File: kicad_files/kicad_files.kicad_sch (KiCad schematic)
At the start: 12 parts, among them J1 Battery Connection, J2 Servo Connection, J3 DC Motor Connection, J4 Washout Ultrasonic Sensor Con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, J5 Water Sensor Connection, J6 Servo Connection, J7 Larvicide Level Ultrasonic Se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

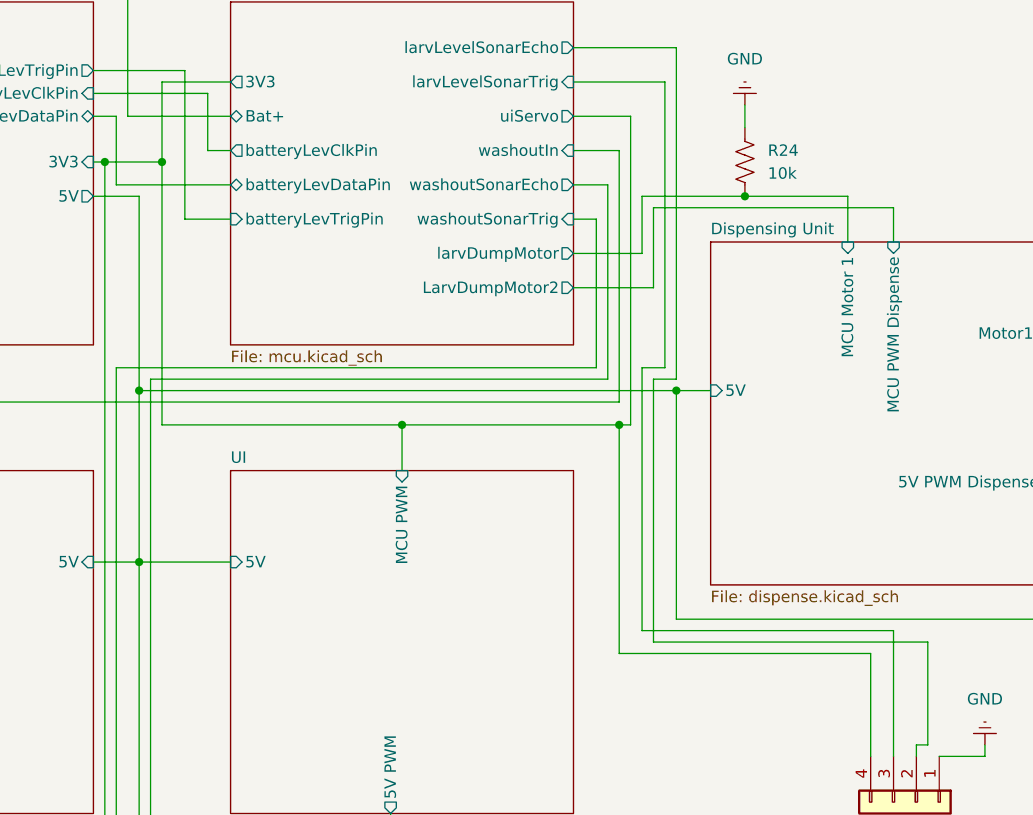
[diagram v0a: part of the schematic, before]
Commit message: Schematic and Footprint error fix
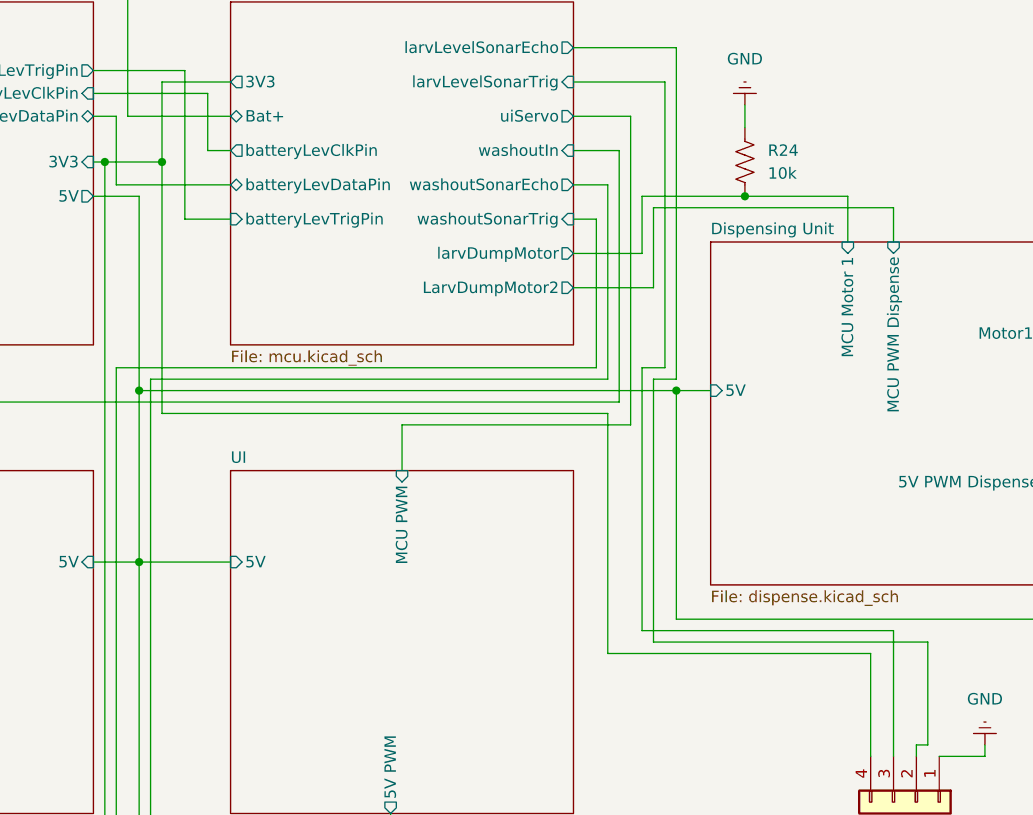
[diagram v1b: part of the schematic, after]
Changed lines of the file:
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@@
-	)
-	(junction
-		(at 140.97 110.49)
-		(diameter 0)
-		(color 0 0 0 0)
 	)
 	(junction
@@
 	)
 	(junction
-		(at 116.84 110.49)
-		(diameter 0)
-		(color 0 0 0 0)
-	)
-	(junction
 		(at 90.17 81.28)
 		(diameter 0)
@@
 	(wire
 		(pts
-			(xy 168.91 135.89) (xy 140.97 135.89)
+			(xy 139.7 135.89) (xy 168.91 135.89)
 		)
 		(stroke
@@
 	(wire
 		(pts
+			(xy 116.84 110.49) (xy 142.24 110.49)
+		)
+		(stroke
+			(width 0)
+			(type default)
+		)
+	)
+	(wire
+		(pts
 			(xy 88.9 105.41) (xy 88.9 173.99)
 		)
@@
 	(wire
 		(pts
+			(xy 90.17 109.22) (xy 90.17 81.28)
+		)
+		(stroke
+			(width 0)
+			(type default)
+		)
+	)
+	(wire
+		(pts
 			(xy 181.61 147.32) (xy 176.53 147.32)
 		)
@@
 	(wire
 		(pts
-			(xy 90.17 110.49) (xy 90.17 81.28)
-		)
-		(stroke
-			(width 0)
-			(type default)
-		)
-	)
-	(wire
-		(pts
 			(xy 195.58 116.84) (xy 189.23 116.84)
 		)
@@
 	(wire
 		(pts
-			(xy 140.97 135.89) (xy 140.97 110.49)
-		)
-		(stroke
-			(width 0)
-			(type default)
-		)
-	)
-	(wire
-		(pts
 			(xy 175.26 134.62) (xy 175.26 146.05)
 		)
@@
 	(wire
 		(pts
-			(xy 90.17 110.49) (xy 116.84 110.49)
-		)
-		(stroke
-			(width 0)
-			(type default)
-		)
-	)
-	(wire
-		(pts
 			(xy 115.57 153.67) (xy 115.57 168.91)
 		)
@@
 	(wire
 		(pts
+			(xy 139.7 135.89) (xy 139.7 109.22)
+		)
+		(stroke
+			(width 0)
+			(type default)
+		)
+	)
+	(wire
+		(pts
 			(xy 87.63 173.99) (xy 87.63 175.26)
 		)
@@
 	(wire
 		(pts
-			(xy 116.84 110.49) (xy 140.97 110.49)
-		)
-		(stroke
-			(width 0)
-			(type default)
-		)
-	)
-	(wire
-		(pts
 			(xy 92.71 71.12) (xy 92.71 87.63)
 		)
@@
 	(wire
 		(pts
+			(xy 139.7 109.22) (xy 90.17 109.22)
+		)
+		(stroke
+			(width 0)
+			(type default)
+		)
+	)
+	(wire
+		(pts
 			(xy 173.99 146.05) (xy 173.99 147.32)
 		)
@@
 		)
 		(stroke
-			(width 0)
-			(type default)
-		)
-	)
-	(wire
-		(pts
-			(xy 140.97 110.49) (xy 142.24 110.49)
-		)
-		(stroke
